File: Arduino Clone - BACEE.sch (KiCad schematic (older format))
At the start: 0 parts

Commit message: Created new child sheet, added proj symbols
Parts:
- added BT?: Battery, symbol Device:Battery
- added C? (x2): C, symbol Device:C
- added C?: CP, symbol Device:CP
- added D?: LED, symbol Device:LED
- added R? (x2): R, symbol Device:R
- added U?: 24LC1025, symbol Memory_EEPROM:24LC1025
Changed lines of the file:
@@
 $Descr A4 11693 8268
 encoding utf-8
-Sheet 1 1
+Sheet 1 2
 Title "Arduino Clone (BACCE)"
 Date "2020-04-05"
@@
 Comment4 ""
 $EndDescr
+$Comp
+L Device:Battery BT?
+U 1 1 5E8CB984
+P 4050 3500
+F 0 "BT?" H 4158 3546 50  0000 L CNN
+F 1 "Battery" H 4158 3455 50  0000 L CNN
+F 2 "" V 4050 3560 50  0001 C CNN
+F 3 "~" V 4050 3560 50  0001 C CNN
+	1    4050 3500
+	1    0    0    -1
+$EndComp
+$Comp
+L Device:C C?
+U 1 1 5E8CCB16
+P 4550 3450
+F 0 "C?" H 4665 3496 50  0000 L CNN
+F 1 "C" H 4665 3405 50  0000 L CNN
+F 2 "" H 4588 3300 50  0001 C CNN
+F 3 "~" H 4550 3450 50  0001 C CNN
+	1    4550 3450
+	1    0    0    -1
+$EndComp
+$Comp
+L Device:C C?
+U 1 1 5E8CD3D9
+P 4550 3850
+F 0 "C?" H 4665 3896 50  0000 L CNN
+F 1 "C" H 4665 3805 50  0000 L CNN
+F 2 "" H 4588 3700 50  0001 C CNN
+F 3 "~" H 4550 3850 50  0001 C CNN
+	1    4550 3850
+	1    0    0    -1
+$EndComp
+$Comp
+L Device:CP C?
+U 1 1 5E8CD911
+P 4550 4350
+F 0 "C?" H 4668 4396 50  0000 L CNN
+F 1 "CP" H 4668 4305 50  0000 L CNN
+F 2 "" H 4588 4200 50  0001 C CNN
+F 3 "~" H 4550 4350 50  0001 C CNN
+	1    4550 4350
+	1    0    0    -1
+$EndComp
+$Comp
+L Device:LED D?
+U 1 1 5E8CE1F4
+P 4050 4250
+F 0 "D?" H 4043 4466 50  0000 C CNN
+F 1 "LED" H 4043 4375 50  0000 C CNN
+F 2 "" H 4050 4250 50  0001 C CNN
+F 3 "~" H 4050 4250 50  0001 C CNN
+	1    4050 4250
+	1    0    0    -1
+$EndComp
+$Comp
+L Device:R R?
+U 1 1 5E8CECF6
+P 5050 3450
+F 0 "R?" H 5120 3496 50  0000 L CNN
+F 1 "R" H 5120 3405 50  0000 L CNN
+F 2 "" V 4980 3450 50  0001 C CNN
+F 3 "~" H 5050 3450 50  0001 C CNN
+	1    5050 3450
+	1    0    0    -1
+$EndComp
+$Comp
+L Device:R R?
+U 1 1 5E8CF356
+P 5050 3850
+F 0 "R?" H 5120 3896 50  0000 L CNN
+F 1 "R" H 5120 3805 50  0000 L CNN
+F 2 "" V 4980 3850 50  0001 C CNN
+F 3 "~" H 5050 3850 50  0001 C CNN
+	1    5050 3850
+	1    0    0    -1
+$EndComp
+$Comp
+L Memory_EEPROM:24LC1025 U?
+U 1 1 5E8CF87B
+P 5800 3550
+F 0 "U?" H 5800 4031 50  0000 C CNN
+F 1 "24LC1025" H 5800 3940 50  0000 C CNN
+F 2 "" H 5800 3550 50  0001 C CNN
+F 3 "http://ww1.microchip.com/downloads/en/DeviceDoc/21941B.pdf" H 5800 3550 50  0001 C CNN
+	1    5800 3550
+	1    0    0    -1
+$EndComp
+$Sheet
+S 5300 4050 1250 950
+U 5E8D09E0
+F0 "Connectors" 50
+F1 "Connectors.sch" 50
+$EndSheet
 $EndSCHEMATC

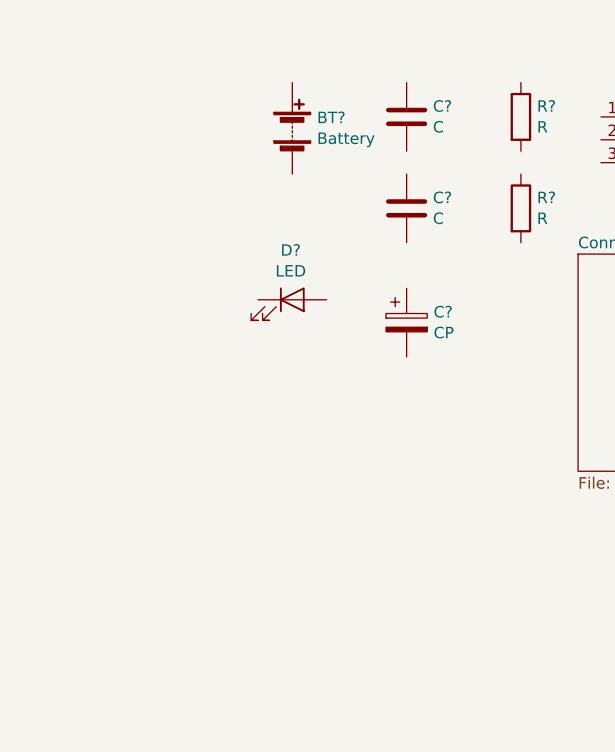
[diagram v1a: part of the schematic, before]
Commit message: Added symbol for atmega328p-au
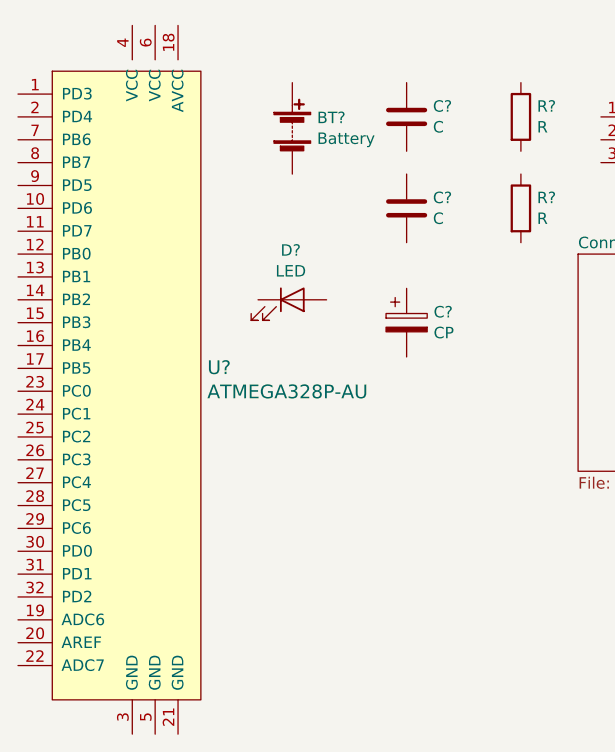
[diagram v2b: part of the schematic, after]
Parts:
- added U?: ATMEGA328P-AU, digikey-footprints:TQFP-32_7x7mm, symbol dk_Embedded-Microcontrollers:ATMEGA328P-AU
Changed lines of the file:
@@
 F1 "Connectors.sch" 50
 $EndSheet
+$Comp
+L dk_Embedded-Microcontrollers:ATMEGA328P-AU U?
+U 1 1 5E8D5484
+P 3350 4650
+F 0 "U?" H 3678 4753 60  0000 L CNN
+F 1 "ATMEGA328P-AU" H 3678 4647 60  0000 L CNN
+F 2 "digikey-footprints:TQFP-32_7x7mm" H 3550 4850 60  0001 L CNN
+F 3 "http://www.microchip.com/mymicrochip/filehandler.aspx?ddocname=en608326" H 3550 4950 60  0001 L CNN
+F 4 "ATMEGA328P-AU-ND" H 3550 5050 60  0001 L CNN "Digi-Key_PN"
+F 5 "ATMEGA328P-AU" H 3550 5150 60  0001 L CNN "MPN"
+F 6 "Integrated Circuits (ICs)" H 3550 5250 60  0001 L CNN "Category"
+F 7 "Embedded - Microcontrollers" H 3550 5350 60  0001 L CNN "Family"
+F 8 "http://www.microchip.com/mymicrochip/filehandler.aspx?ddocname=en608326" H 3550 5450 60  0001 L CNN "DK_Datasheet_Link"
+F 9 "/product-detail/en/microchip-technology/ATMEGA328P-AU/ATMEGA328P-AU-ND/1832260" H 3550 5550 60  0001 L CNN "DK_Detail_Page"
+F 10 "IC MCU 8BIT 32KB FLASH 32TQFP" H 3550 5650 60  0001 L CNN "Description"
+F 11 "Microchip Technology" H 3550 5750 60  0001 L CNN "Manufacturer"
+F 12 "Active" H 3550 5850 60  0001 L CNN "Status"
+	1    3350 4650
+	1    0    0    -1
+$EndComp
 $EndSCHEMATC

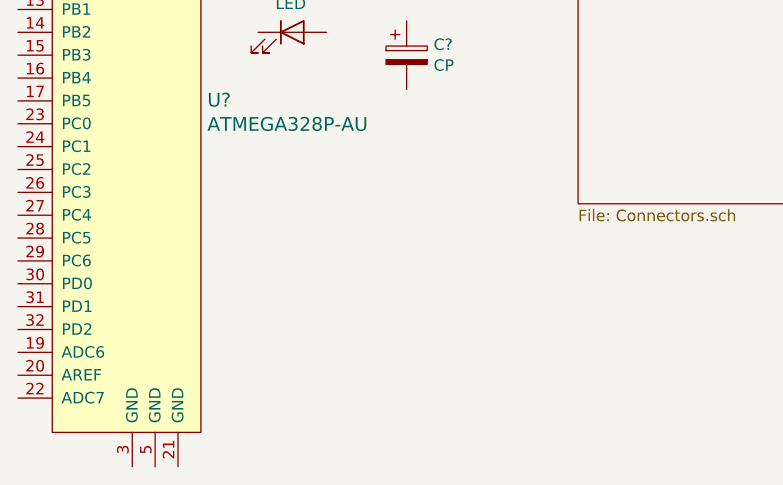
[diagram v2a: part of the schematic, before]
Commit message: Added clock IC custom
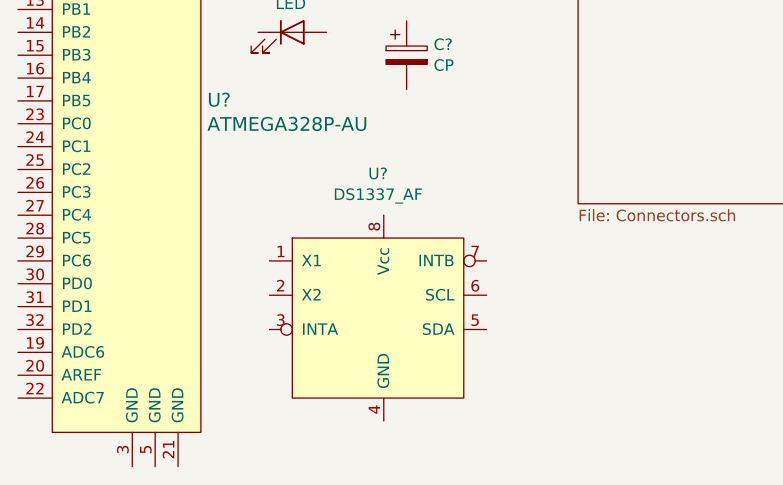
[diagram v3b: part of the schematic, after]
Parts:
- added U?: DS1337_AF, symbol proj3:DS1337_AF
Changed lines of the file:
@@
+	1    0    0    -1
+$EndComp
+$Comp
+L proj3:DS1337_AF U?
+U 1 1 5E8DA0DF
+P 4450 5500
+F 0 "U?" H 4425 6131 50  0000 C CNN
+F 1 "DS1337_AF" H 4425 6040 50  0000 C CNN
+F 2 "" H 4450 5500 50  0001 C CNN
+F 3 "https://datasheets.maximintegrated.com/en/ds/DS1337-DS1337C.pdf" H 4450 5500 50  0001 C CNN
+	1    4450 5500
 	1    0    0    -1
 $EndComp

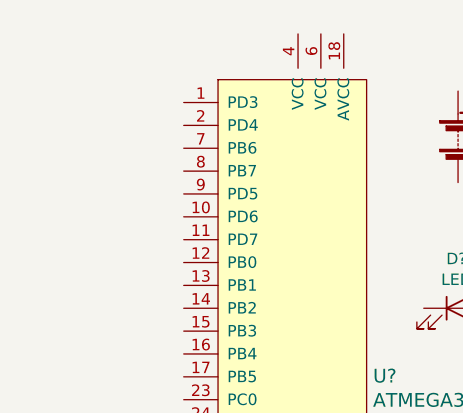
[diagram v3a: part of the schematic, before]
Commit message: Added missing crystal
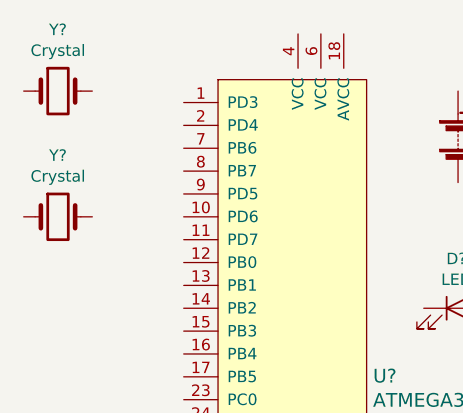
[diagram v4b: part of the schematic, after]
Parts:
- added Y? (x2): Crystal, symbol Device:Crystal
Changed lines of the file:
@@
+	1    0    0    -1
+$EndComp
+$Comp
+L Device:Crystal Y?
+U 1 1 5E8DB304
+P 2300 3300
+F 0 "Y?" H 2300 3568 50  0000 C CNN
+F 1 "Crystal" H 2300 3477 50  0000 C CNN
+F 2 "" H 2300 3300 50  0001 C CNN
+F 3 "~" H 2300 3300 50  0001 C CNN
+	1    2300 3300
+	1    0    0    -1
+$EndComp
+$Comp
+L Device:Crystal Y?
+U 1 1 5E8DC7C9
+P 2300 3850
+F 0 "Y?" H 2300 4118 50  0000 C CNN
+F 1 "Crystal" H 2300 4027 50  0000 C CNN
+F 2 "" H 2300 3850 50  0001 C CNN
+F 3 "~" H 2300 3850 50  0001 C CNN
+	1    2300 3850
 	1    0    0    -1
 $EndComp

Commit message: symbol rearrangement
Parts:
- added U?: 24LC1025, symbol Memory_EEPROM:24LC1025
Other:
- moved on the sheet: BT?, C?, D?, R?, U?, Y?
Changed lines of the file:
@@
 L Device:Battery BT?
 U 1 1 5E8CB984
-P 4050 3500
-F 0 "BT?" H 4158 3546 50  0000 L CNN
-F 1 "Battery" H 4158 3455 50  0000 L CNN
-F 2 "" V 4050 3560 50  0001 C CNN
-F 3 "~" V 4050 3560 50  0001 C CNN
-	1    4050 3500
+P 9100 2250
+F 0 "BT?" H 9208 2296 50  0000 L CNN
+F 1 "Battery" H 9208 2205 50  0000 L CNN
+F 2 "" V 9100 2310 50  0001 C CNN
+F 3 "~" V 9100 2310 50  0001 C CNN
+	1    9100 2250
 	1    0    0    -1
 $EndComp
@@
 L Device:C C?
 U 1 1 5E8CCB16
-P 4550 3450
-F 0 "C?" H 4665 3496 50  0000 L CNN
-F 1 "C" H 4665 3405 50  0000 L CNN
-F 2 "" H 4588 3300 50  0001 C CNN
-F 3 "~" H 4550 3450 50  0001 C CNN
-	1    4550 3450
+P 5300 1850
+F 0 "C?" H 5415 1896 50  0000 L CNN
+F 1 "C" H 5415 1805 50  0000 L CNN
+F 2 "" H 5338 1700 50  0001 C CNN
+F 3 "~" H 5300 1850 50  0001 C CNN
+	1    5300 1850
 	1    0    0    -1
 $EndComp
@@
 L Device:C C?
 U 1 1 5E8CD3D9
-P 4550 3850
-F 0 "C?" H 4665 3896 50  0000 L CNN
-F 1 "C" H 4665 3805 50  0000 L CNN
-F 2 "" H 4588 3700 50  0001 C CNN
-F 3 "~" H 4550 3850 50  0001 C CNN
-	1    4550 3850
+P 5300 2250
+F 0 "C?" H 5415 2296 50  0000 L CNN
+F 1 "C" H 5415 2205 50  0000 L CNN
+F 2 "" H 5338 2100 50  0001 C CNN
+F 3 "~" H 5300 2250 50  0001 C CNN
+	1    5300 2250
 	1    0    0    -1
 $EndComp
@@
 L Device:CP C?
 U 1 1 5E8CD911
-P 4550 4350
-F 0 "C?" H 4668 4396 50  0000 L CNN
-F 1 "CP" H 4668 4305 50  0000 L CNN
-F 2 "" H 4588 4200 50  0001 C CNN
-F 3 "~" H 4550 4350 50  0001 C CNN
-	1    4550 4350
+P 9600 3100
+F 0 "C?" H 9718 3146 50  0000 L CNN
+F 1 "CP" H 9718 3055 50  0000 L CNN
+F 2 "" H 9638 2950 50  0001 C CNN
+F 3 "~" H 9600 3100 50  0001 C CNN
+	1    9600 3100
 	1    0    0    -1
 $EndComp
@@
 L Device:LED D?
 U 1 1 5E8CE1F4
-P 4050 4250
-F 0 "D?" H 4043 4466 50  0000 C CNN
-F 1 "LED" H 4043 4375 50  0000 C CNN
-F 2 "" H 4050 4250 50  0001 C CNN
-F 3 "~" H 4050 4250 50  0001 C CNN
-	1    4050 4250
+P 5850 2650
+F 0 "D?" H 5843 2866 50  0000 C CNN
+F 1 "LED" H 5843 2775 50  0000 C CNN
+F 2 "" H 5850 2650 50  0001 C CNN
+F 3 "~" H 5850 2650 50  0001 C CNN
+	1    5850 2650
 	1    0    0    -1
 $EndComp
@@
 L Device:R R?
 U 1 1 5E8CECF6
-P 5050 3450
-F 0 "R?" H 5120 3496 50  0000 L CNN
-F 1 "R" H 5120 3405 50  0000 L CNN
-F 2 "" V 4980 3450 50  0001 C CNN
-F 3 "~" H 5050 3450 50  0001 C CNN
-	1    5050 3450
+P 5400 2950
+F 0 "R?" H 5470 2996 50  0000 L CNN
+F 1 "R" H 5470 2905 50  0000 L CNN
+F 2 "" V 5330 2950 50  0001 C CNN
+F 3 "~" H 5400 2950 50  0001 C CNN
+	1    5400 2950
 	1    0    0    -1
 $EndComp
@@
 L Device:R R?
 U 1 1 5E8CF356
-P 5050 3850
-F 0 "R?" H 5120 3896 50  0000 L CNN
-F 1 "R" H 5120 3805 50  0000 L CNN
-F 2 "" V 4980 3850 50  0001 C CNN
-F 3 "~" H 5050 3850 50  0001 C CNN
-	1    5050 3850
+P 5400 3350
+F 0 "R?" H 5470 3396 50  0000 L CNN
+F 1 "R" H 5470 3305 50  0000 L CNN
+F 2 "" V 5330 3350 50  0001 C CNN
+F 3 "~" H 5400 3350 50  0001 C CNN
+	1    5400 3350
 	1    0    0    -1
 $EndComp
@@
 L Memory_EEPROM:24LC1025 U?
 U 1 1 5E8CF87B
-P 5800 3550
-F 0 "U?" H 5800 4031 50  0000 C CNN
-F 1 "24LC1025" H 5800 3940 50  0000 C CNN
-F 2 "" H 5800 3550 50  0001 C CNN
-F 3 "http://ww1.microchip.com/downloads/en/DeviceDoc/21941B.pdf" H 5800 3550 50  0001 C CNN
-	1    5800 3550
+P 2100 5350
+F 0 "U?" H 2100 5831 50  0000 C CNN
+F 1 "24LC1025" H 2100 5740 50  0000 C CNN
+F 2 "" H 2100 5350 50  0001 C CNN
+F 3 "http://ww1.microchip.com/downloads/en/DeviceDoc/21941B.pdf" H 2100 5350 50  0001 C CNN
+	1    2100 5350
 	1    0    0    -1
 $EndComp
 $Sheet
-S 5300 4050 1250 950
+S 5150 6400 1250 950
 U 5E8D09E0
 F0 "Connectors" 50
@@
 L dk_Embedded-Microcontrollers:ATMEGA328P-AU U?
 U 1 1 5E8D5484
-P 3350 4650
-F 0 "U?" H 3678 4753 60  0000 L CNN
-F 1 "ATMEGA328P-AU" H 3678 4647 60  0000 L CNN
-F 2 "digikey-footprints:TQFP-32_7x7mm" H 3550 4850 60  0001 L CNN
-F 3 "http://www.microchip.com/mymicrochip/filehandler.aspx?ddocname=en608326" H 3550 4950 60  0001 L CNN
-F 4 "ATMEGA328P-AU-ND" H 3550 5050 60  0001 L CNN "Digi-Key_PN"
-F 5 "ATMEGA328P-AU" H 3550 5150 60  0001 L CNN "MPN"
-F 6 "Integrated Circuits (ICs)" H 3550 5250 60  0001 L CNN "Category"
-F 7 "Embedded - Microcontrollers" H 3550 5350 60  0001 L CNN "Family"
-F 8 "http://www.microchip.com/mymicrochip/filehandler.aspx?ddocname=en608326" H 3550 5450 60  0001 L CNN "DK_Datasheet_Link"
-F 9 "/product-detail/en/microchip-technology/ATMEGA328P-AU/ATMEGA328P-AU-ND/1832260" H 3550 5550 60  0001 L CNN "DK_Detail_Page"
-F 10 "IC MCU 8BIT 32KB FLASH 32TQFP" H 3550 5650 60  0001 L CNN "Description"
-F 11 "Microchip Technology" H 3550 5750 60  0001 L CNN "Manufacturer"
-F 12 "Active" H 3550 5850 60  0001 L CNN "Status"
-	1    3350 4650
+P 7050 3050
+F 0 "U?" H 7378 3153 60  0000 L CNN
+F 1 "ATMEGA328P-AU" H 7378 3047 60  0000 L CNN
+F 2 "digikey-footprints:TQFP-32_7x7mm" H 7250 3250 60  0001 L CNN
+F 3 "http://www.microchip.com/mymicrochip/filehandler.aspx?ddocname=en608326" H 7250 3350 60  0001 L CNN
+F 4 "ATMEGA328P-AU-ND" H 7250 3450 60  0001 L CNN "Digi-Key_PN"
+F 5 "ATMEGA328P-AU" H 7250 3550 60  0001 L CNN "MPN"
+F 6 "Integrated Circuits (ICs)" H 7250 3650 60  0001 L CNN "Category"
+F 7 "Embedded - Microcontrollers" H 7250 3750 60  0001 L CNN "Family"
+F 8 "http://www.microchip.com/mymicrochip/filehandler.aspx?ddocname=en608326" H 7250 3850 60  0001 L CNN "DK_Datasheet_Link"
+F 9 "/product-detail/en/microchip-technology/ATMEGA328P-AU/ATMEGA328P-AU-ND/1832260" H 7250 3950 60  0001 L CNN "DK_Detail_Page"
+F 10 "IC MCU 8BIT 32KB FLASH 32TQFP" H 7250 4050 60  0001 L CNN "Description"
+F 11 "Microchip Technology" H 7250 4150 60  0001 L CNN "Manufacturer"
+F 12 "Active" H 7250 4250 60  0001 L CNN "Status"
+	1    7050 3050
 	1    0    0    -1
 $EndComp
@@
 L proj3:DS1337_AF U?
 U 1 1 5E8DA0DF
-P 4450 5500
-F 0 "U?" H 4425 6131 50  0000 C CNN
-F 1 "DS1337_AF" H 4425 6040 50  0000 C CNN
-F 2 "" H 4450 5500 50  0001 C CNN
-F 3 "https://datasheets.maximintegrated.com/en/ds/DS1337-DS1337C.pdf" H 4450 5500 50  0001 C CNN
-	1    4450 5500
+P 2550 2250
+F 0 "U?" H 2525 2881 50  0000 C CNN
+F 1 "DS1337_AF" H 2525 2790 50  0000 C CNN
+F 2 "" H 2550 2250 50  0001 C CNN
+F 3 "https://datasheets.maximintegrated.com/en/ds/DS1337-DS1337C.pdf" H 2550 2250 50  0001 C CNN
+	1    2550 2250
 	1    0    0    -1
 $EndComp
@@
 L Device:Crystal Y?
 U 1 1 5E8DB304
-P 2300 3300
-F 0 "Y?" H 2300 3568 50  0000 C CNN
-F 1 "Crystal" H 2300 3477 50  0000 C CNN
-F 2 "" H 2300 3300 50  0001 C CNN
-F 3 "~" H 2300 3300 50  0001 C CNN
-	1    2300 3300
+P 1600 2000
+F 0 "Y?" H 1600 2268 50  0000 C CNN
+F 1 "Crystal" H 1600 2177 50  0000 C CNN
+F 2 "" H 1600 2000 50  0001 C CNN
+F 3 "~" H 1600 2000 50  0001 C CNN
+	1    1600 2000
 	1    0    0    -1
 $EndComp
@@
 L Device:Crystal Y?
 U 1 1 5E8DC7C9
-P 2300 3850
-F 0 "Y?" H 2300 4118 50  0000 C CNN
-F 1 "Crystal" H 2300 4027 50  0000 C CNN
-F 2 "" H 2300 3850 50  0001 C CNN
-F 3 "~" H 2300 3850 50  0001 C CNN
-	1    2300 3850
+P 5750 2100
+F 0 "Y?" V 5704 2231 50  0000 L CNN
+F 1 "Crystal" V 5795 2231 50  0000 L CNN
+F 2 "" H 5750 2100 50  0001 C CNN
+F 3 "~" H 5750 2100 50  0001 C CNN
+	1    5750 2100
+	0    1    1    0
+$EndComp
+$Comp
+L Memory_EEPROM:24LC1025 U?
+U 1 1 5E8E407A
+P 2100 6500
+F 0 "U?" H 2100 6981 50  0000 C CNN
+F 1 "24LC1025" H 2100 6890 50  0000 C CNN
+F 2 "" H 2100 6500 50  0001 C CNN
+F 3 "http://ww1.microchip.com/downloads/en/DeviceDoc/21941B.pdf" H 2100 6500 50  0001 C CNN
+	1    2100 6500
 	1    0    0    -1
 $EndComp
+$Comp
+L power:GND #PWR?
+U 1 1 5E8F4304
+P 9450 3400
+F 0 "#PWR?" H 9450 3150 50  0001 C CNN
+F 1 "GND" H 9455 3227 50  0000 C CNN
+F 2 "" H 9450 3400 50  0001 C CNN
+F 3 "" H 9450 3400 50  0001 C CNN
+	1    9450 3400
+	1    0    0    -1
+$EndComp

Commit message: Annotate
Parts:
- gave numbers to parts that had none: 13
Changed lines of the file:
@@
 $EndDescr
 $Comp
-L Device:Battery BT?
+L Device:Battery BT1
 U 1 1 5E8CB984
 P 9100 2250
-F 0 "BT?" H 9208 2296 50  0000 L CNN
+F 0 "BT1" H 9208 2296 50  0000 L CNN
 F 1 "Battery" H 9208 2205 50  0000 L CNN
 F 2 "" V 9100 2310 50  0001 C CNN
@@
 $EndComp
 $Comp
-L Device:C C?
+L Device:C C1
 U 1 1 5E8CCB16
 P 5300 1850
-F 0 "C?" H 5415 1896 50  0000 L CNN
+F 0 "C1" H 5415 1896 50  0000 L CNN
 F 1 "C" H 5415 1805 50  0000 L CNN
 F 2 "" H 5338 1700 50  0001 C CNN
@@
 $EndComp
 $Comp
-L Device:C C?
+L Device:C C2
 U 1 1 5E8CD3D9
 P 5300 2250
-F 0 "C?" H 5415 2296 50  0000 L CNN
+F 0 "C2" H 5415 2296 50  0000 L CNN
 F 1 "C" H 5415 2205 50  0000 L CNN
 F 2 "" H 5338 2100 50  0001 C CNN
@@
 $EndComp
 $Comp
-L Device:CP C?
+L Device:CP C3
 U 1 1 5E8CD911
 P 9600 3100
-F 0 "C?" H 9718 3146 50  0000 L CNN
+F 0 "C3" H 9718 3146 50  0000 L CNN
 F 1 "CP" H 9718 3055 50  0000 L CNN
 F 2 "" H 9638 2950 50  0001 C CNN
@@
 $EndComp
 $Comp
-L Device:LED D?
+L Device:LED D1
 U 1 1 5E8CE1F4
 P 5850 2650
-F 0 "D?" H 5843 2866 50  0000 C CNN
+F 0 "D1" H 5843 2866 50  0000 C CNN
 F 1 "LED" H 5843 2775 50  0000 C CNN
 F 2 "" H 5850 2650 50  0001 C CNN
@@
 $EndComp
 $Comp
-L Device:R R?
+L Device:R R1
 U 1 1 5E8CECF6
 P 5400 2950
-F 0 "R?" H 5470 2996 50  0000 L CNN
+F 0 "R1" H 5470 2996 50  0000 L CNN
 F 1 "R" H 5470 2905 50  0000 L CNN
 F 2 "" V 5330 2950 50  0001 C CNN
@@
 $EndComp
 $Comp
-L Device:R R?
+L Device:R R2
 U 1 1 5E8CF356
 P 5400 3350
-F 0 "R?" H 5470 3396 50  0000 L CNN
+F 0 "R2" H 5470 3396 50  0000 L CNN
 F 1 "R" H 5470 3305 50  0000 L CNN
 F 2 "" V 5330 3350 50  0001 C CNN
@@
 $EndComp
 $Comp
-L Memory_EEPROM:24LC1025 U?
+L Memory_EEPROM:24LC1025 U1
 U 1 1 5E8CF87B
 P 2100 5350
-F 0 "U?" H 2100 5831 50  0000 C CNN
+F 0 "U1" H 2100 5831 50  0000 C CNN
 F 1 "24LC1025" H 2100 5740 50  0000 C CNN
 F 2 "" H 2100 5350 50  0001 C CNN
@@
 $EndSheet
 $Comp
-L dk_Embedded-Microcontrollers:ATMEGA328P-AU U?
+L dk_Embedded-Microcontrollers:ATMEGA328P-AU U4
 U 1 1 5E8D5484
 P 7050 3050
-F 0 "U?" H 7378 3153 60  0000 L CNN
+F 0 "U4" H 7378 3153 60  0000 L CNN
 F 1 "ATMEGA328P-AU" H 7378 3047 60  0000 L CNN
 F 2 "digikey-footprints:TQFP-32_7x7mm" H 7250 3250 60  0001 L CNN
@@
 $EndComp
 $Comp
-L proj3:DS1337_AF U?
+L proj3:DS1337_AF U3
 U 1 1 5E8DA0DF
 P 2550 2250
-F 0 "U?" H 2525 2881 50  0000 C CNN
+F 0 "U3" H 2525 2881 50  0000 C CNN
 F 1 "DS1337_AF" H 2525 2790 50  0000 C CNN
 F 2 "" H 2550 2250 50  0001 C CNN
@@
 $EndComp
 $Comp
-L Device:Crystal Y?
+L Device:Crystal Y1
 U 1 1 5E8DB304
 P 1600 2000
-F 0 "Y?" H 1600 2268 50  0000 C CNN
+F 0 "Y1" H 1600 2268 50  0000 C CNN
 F 1 "Crystal" H 1600 2177 50  0000 C CNN
 F 2 "" H 1600 2000 50  0001 C CNN
@@
 $EndComp
 $Comp
-L Device:Crystal Y?
+L Device:Crystal Y2
 U 1 1 5E8DC7C9
 P 5750 2100
-F 0 "Y?" V 5704 2231 50  0000 L CNN
+F 0 "Y2" V 5704 2231 50  0000 L CNN
 F 1 "Crystal" V 5795 2231 50  0000 L CNN
 F 2 "" H 5750 2100 50  0001 C CNN
@@
 $EndComp
 $Comp
-L Memory_EEPROM:24LC1025 U?
+L Memory_EEPROM:24LC1025 U2
 U 1 1 5E8E407A
 P 2100 6500
-F 0 "U?" H 2100 6981 50  0000 C CNN
+F 0 "U2" H 2100 6981 50  0000 C CNN
 F 1 "24LC1025" H 2100 6890 50  0000 C CNN
 F 2 "" H 2100 6500 50  0001 C CNN
@@
 $EndComp
 $Comp
-L power:GND #PWR?
+L power:GND #PWR01
 U 1 1 5E8F4304
 P 9450 3400
-F 0 "#PWR?" H 9450 3150 50  0001 C CNN
+F 0 "#PWR01" H 9450 3150 50  0001 C CNN
 F 1 "GND" H 9455 3227 50  0000 C CNN
 F 2 "" H 9450 3400 50  0001 C CNN
